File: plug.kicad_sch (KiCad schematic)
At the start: 30 parts, among them J10 Conn_01x04_GH1.25, J11 Conn_01x04_GH1.25, J12 Conn_01x04_GH1.25, J13 Conn_01x08_GH1.25, J2 Conn_01x02_XH2.54, J3 Conn_01x02_XH2.54, J4 Conn_01x02_XH2.54, J5 Conn_01x02_XH2.54, J6 KF2EDGR-3.81-2P, J7 Conn_01x04_GH1.25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

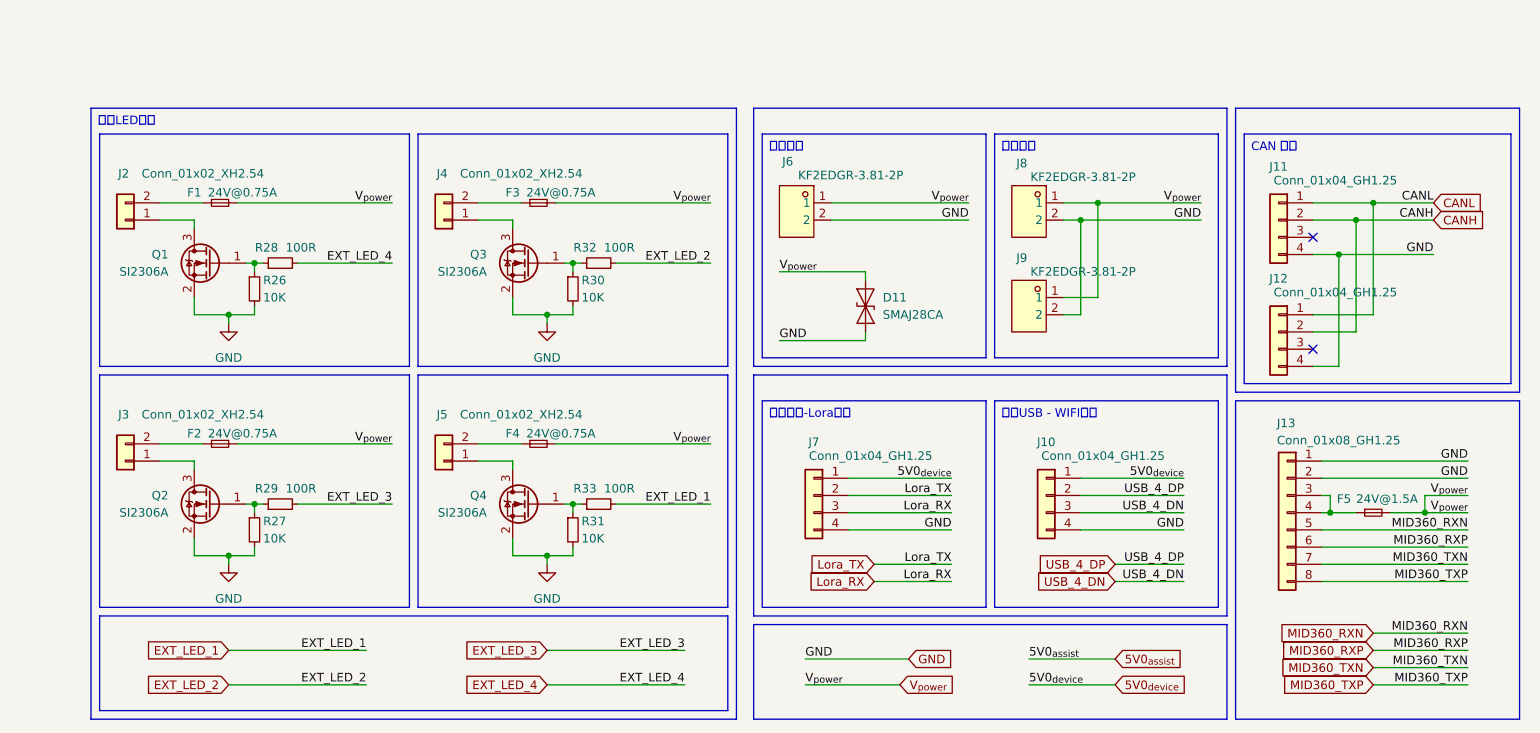
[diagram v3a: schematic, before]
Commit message: pref: USB外设改自供电，优化布线
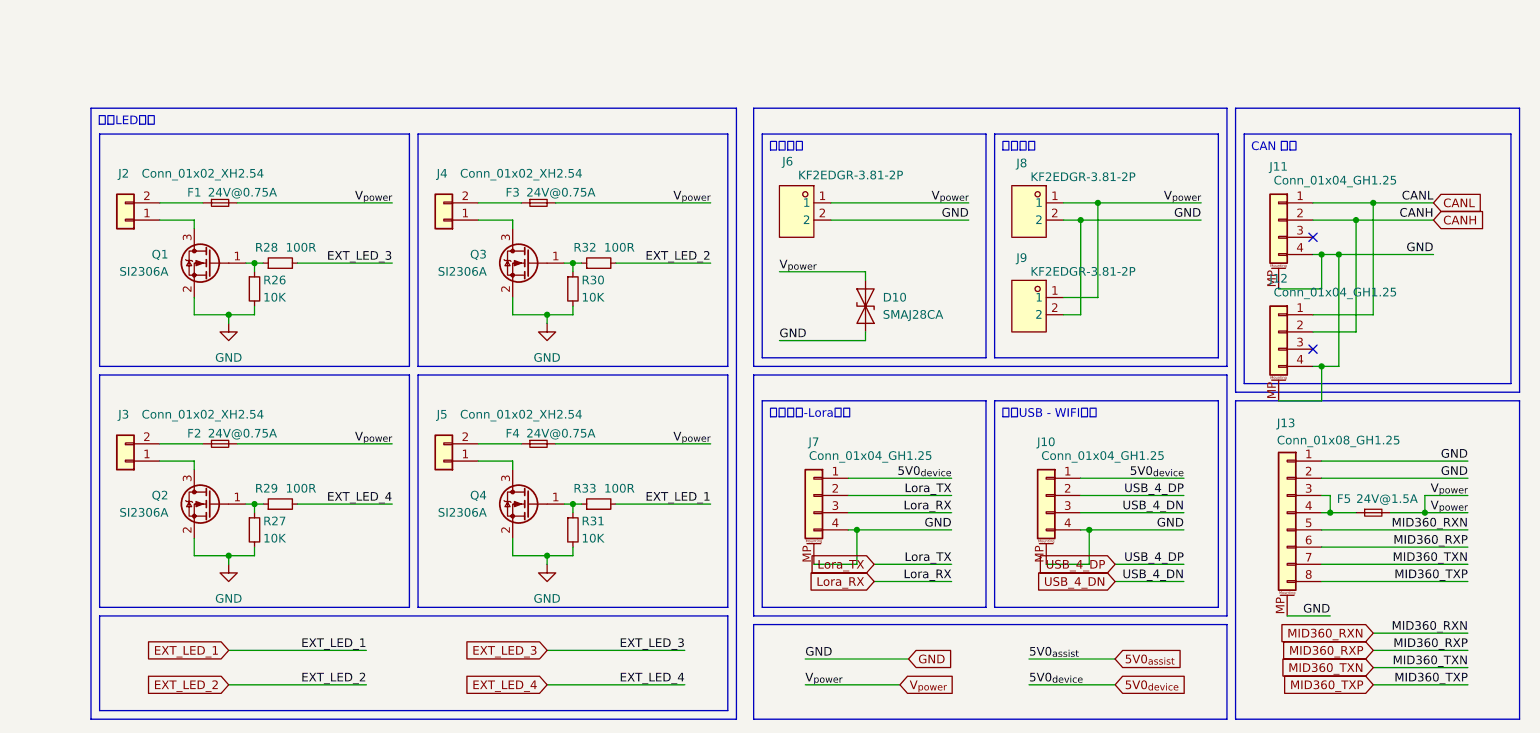
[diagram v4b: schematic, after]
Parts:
- J10, J11, J12, J7: symbol Connector_Generic:Conn_01x04 -> Connector_Generic_MountingPin:Conn_01x04_MountingPin
- J13: symbol Connector_Generic:Conn_01x08 -> Connector_Generic_MountingPin:Conn_01x08_MountingPin
- renumbered D11 to D10
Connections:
- net EXT_LED_3: now also R28.2; no longer R29.2
- net EXT_LED_4: now also R29.2; no longer R28.2
- net GND: now also J10.MP (MountPin), J11.MP (MountPin), J12.MP (MountPin), J13.MP (MountPin), J7.MP (MountPin)
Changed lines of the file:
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@@
 	)
 	(junction
+		(at 212.09 57.15)
+		(diameter 0)
+		(color 0 0 0 0)
+	)
+	(junction
+		(at 177.8 97.79)
+		(diameter 0)
+		(color 0 0 0 0)
+	)
+	(junction
 		(at 50.8 66.04)
 		(diameter 0)
@@
 	)
 	(junction
+		(at 212.09 73.66)
+		(diameter 0)
+		(color 0 0 0 0)
+	)
+	(junction
 		(at 101.6 58.42)
 		(diameter 0)
@@
 	)
 	(junction
+		(at 143.51 97.79)
+		(diameter 0)
+		(color 0 0 0 0)
+	)
+	(junction
 		(at 219.71 49.53)
 		(diameter 0)
@@
 	(wire
 		(pts
+			(xy 212.09 62.23) (xy 212.09 57.15)
+		)
+		(stroke
+			(width 0)
+			(type default)
+		)
+	)
+	(wire
+		(pts
+			(xy 212.09 73.66) (xy 214.63 73.66)
+		)
+		(stroke
+			(width 0)
+			(type default)
+		)
+	)
+	(wire
+		(pts
 			(xy 54.61 95.25) (xy 54.61 93.98)
 		)
@@
 	(wire
 		(pts
+			(xy 212.09 105.41) (xy 233.68 105.41)
+		)
+		(stroke
+			(width 0)
+			(type default)
+		)
+	)
+	(wire
+		(pts
 			(xy 101.6 58.42) (xy 100.33 58.42)
 		)
@@
 	(wire
 		(pts
+			(xy 137.16 102.87) (xy 143.51 102.87)
+		)
+		(stroke
+			(width 0)
+			(type default)
+		)
+	)
+	(wire
+		(pts
 			(xy 99.06 49.53) (xy 121.92 49.53)
 		)
@@
 	(wire
 		(pts
-			(xy 210.82 73.66) (xy 214.63 73.66)
+			(xy 210.82 73.66) (xy 212.09 73.66)
 		)
 		(stroke
@@
 	(wire
 		(pts
-			(xy 142.24 97.79) (xy 157.48 97.79)
+			(xy 142.24 97.79) (xy 143.51 97.79)
 		)
 		(stroke
@@
 	(wire
 		(pts
-			(xy 60.96 93.98) (xy 74.93 93.98)
+			(xy 212.09 78.74) (xy 212.09 73.66)
 		)
 		(stroke
@@
 	(wire
 		(pts
-			(xy 219.71 66.04) (xy 219.71 49.53)
+			(xy 60.96 93.98) (xy 74.93 93.98)
 		)
 		(stroke
@@
 	(wire
 		(pts
-			(xy 212.09 105.41) (xy 233.68 105.41)
+			(xy 219.71 66.04) (xy 219.71 49.53)
 		)
 		(stroke
@@
 	(wire
 		(pts
+			(xy 171.45 102.87) (xy 177.8 102.87)
+		)
+		(stroke
+			(width 0)
+			(type default)
+		)
+	)
+	(wire
+		(pts
 			(xy 168.91 116.84) (xy 181.61 116.84)
 		)
@@
 	(wire
 		(pts
+			(xy 207.01 110.49) (xy 213.36 110.49)
+		)
+		(stroke
+			(width 0)
+			(type default)
+		)
+	)
+	(wire
+		(pts
 			(xy 179.07 63.5) (xy 179.07 49.53)
 		)
@@
 	(wire
 		(pts
+			(xy 143.51 97.79) (xy 157.48 97.79)
+		)
+		(stroke
+			(width 0)
+			(type default)
+		)
+	)
+	(wire
+		(pts
 			(xy 160.02 49.53) (xy 139.7 49.53)
 		)
@@
 	(wire
 		(pts
-			(xy 176.53 97.79) (xy 191.77 97.79)
+			(xy 176.53 97.79) (xy 177.8 97.79)
 		)
 		(stroke
@@
 	(wire
 		(pts
-			(xy 214.63 57.15) (xy 210.82 57.15)
+			(xy 214.63 57.15) (xy 212.09 57.15)
 		)
 		(stroke
@@
 	(wire
 		(pts
+			(xy 205.74 62.23) (xy 212.09 62.23)
+		)
+		(stroke
+			(width 0)
+			(type default)
+		)
+	)
+	(wire
+		(pts
+			(xy 205.74 78.74) (xy 212.09 78.74)
+		)
+		(stroke
+			(width 0)
+			(type default)
+		)
+	)
+	(wire
+		(pts
 			(xy 92.71 88.9) (xy 92.71 87.63)
 		)
@@
 	(wire
 		(pts
+			(xy 143.51 102.87) (xy 143.51 97.79)
+		)
+		(stroke
+			(width 0)
+			(type default)
+		)
+	)
+	(wire
+		(pts
 			(xy 168.91 120.65) (xy 181.61 120.65)
 		)
@@
 	(wire
 		(pts
+			(xy 177.8 97.79) (xy 191.77 97.79)
+		)
+		(stroke
+			(width 0)
+			(type default)
+		)
+	)
+	(wire
+		(pts
 			(xy 142.24 90.17) (xy 157.48 90.17)
 		)
@@
 	(wire
 		(pts
+			(xy 212.09 57.15) (xy 210.82 57.15)
+		)
+		(stroke
+			(width 0)
+			(type default)
+		)
+	)
+	(wire
+		(pts
 			(xy 194.31 49.53) (xy 179.07 49.53)
 		)
@@
 	(wire
 		(pts
+			(xy 177.8 102.87) (xy 177.8 97.79)
+		)
+		(stroke
+			(width 0)
+			(type default)
+		)
+	)
+	(wire
+		(pts
 			(xy 144.78 69.85) (xy 144.78 68.58)
 		)
@@
 	)
 	(label "EXT_LED_4"
-		(at 74.93 58.42 180)
+		(at 74.93 93.98 180)
 		(effects
 			(font
@@
 		)
 	)
+	(label "GND"
+		(at 213.36 110.49 180)
+		(effects
+			(font
+				(size 1.27 1.27)
+			)
+			(justify right bottom)
+		)
+	)
 	(label "MID360_TXP"
 		(at 233.68 120.65 180)
@@
 	)
 	(label "EXT_LED_3"
-		(at 74.93 93.98 180)
+		(at 74.93 58.42 180)
 		(effects
 			(font
@@
 	)
 	(symbol
-		(lib_id "Connector_Generic:Conn_01x04")
+		(lib_id "Connector_Generic_MountingPin:Conn_01x04_MountingPin")
 		(at 205.74 68.58 0)
 		(mirror y)
@@
 			)
 		)
-		(property "Description" "Generic connector, single row, 01x04, script generated (kicad-library-utils/schlib/autogen/connector/)"
+		(property "Description" "Generic connectable mounting pin connector, single row, 01x04, script generated (kicad-library-utils/schlib/autogen/connector/)"
 			(at 205.74 68.58 0)
 			(effects
@@
 		(pin "1"
 		)
+		(pin "MP"
+		)
 		(instances
 			(project "ZW1S"
@@
 		(dnp no)
 		(fields_autoplaced yes)
-		(property "Reference" "#PWR15"
+		(property "Reference" "#PWR16"
 			(at 97.79 73.66 0)
 			(effects
@@
 			(project "ZW1S"
 				(path "/c658c753-a869-4eb9-a520-6b2e7fae7fd9/cfdc2bd0-e52f-4e45-9f57-35a106e1bb09"
-					(reference "#PWR15")
+					(reference "#PWR16")
 					(unit 1)
 				)
@@
 		(dnp no)
 		(fields_autoplaced yes)
-		(property "Reference" "#PWR13"
+		(property "Reference" "#PWR14"
 			(at 50.8 73.66 0)
 			(effects
@@
 			(project ""
 				(path "/c658c753-a869-4eb9-a520-6b2e7fae7fd9/cfdc2bd0-e52f-4e45-9f57-35a106e1bb09"
-					(reference "#PWR13")
+					(reference "#PWR14")
 					(unit 1)
 				)
@@
 	)
 	(symbol
-		(lib_id "Connector_Generic:Conn_01x04")
+		(lib_id "Connector_Generic_MountingPin:Conn_01x04_MountingPin")
 		(at 171.45 92.71 0)
 		(mirror y)
@@
 			)
 		)
-		(property "Description" "Generic connector, single row, 01x04, script generated (kicad-library-utils/schlib/autogen/connector/)"
+		(property "Description" "Generic connectable mounting pin connector, single row, 01x04, script generated (kicad-library-utils/schlib/autogen/connector/)"
 			(at 171.45 92.71 0)
 			(effects
@@
 		(pin "1"
 		)
+		(pin "MP"
+		)
 		(instances
 			(project "ZW1S"
@@
 		(dnp no)
 		(fields_autoplaced yes)
-		(property "Reference" "#PWR16"
+		(property "Reference" "#PWR17"
 			(at 97.79 109.22 0)
 			(effects
@@
 			(project "ZW1S"
 				(path "/c658c753-a869-4eb9-a520-6b2e7fae7fd9/cfdc2bd0-e52f-4e45-9f57-35a106e1bb09"
-					(reference "#PWR16")
+					(reference "#PWR17")
 					(unit 1)
 				)
@@
 	)
 	(symbol
-		(lib_id "Connector_Generic:Conn_01x04")
+		(lib_id "Connector_Generic_MountingPin:Conn_01x04_MountingPin")
 		(at 205.74 52.07 0)
 		(mirror y)
@@
 			)
 		)
-		(property "Description" "Generic connector, single row, 01x04, script generated (kicad-library-utils/schlib/autogen/connector/)"
+		(property "Description" "Generic connectable mounting pin connector, single row, 01x04, script generated (kicad-library-utils/schlib/autogen/connector/)"
 			(at 205.74 52.07 0)
 			(effects
@@
 		(pin "1"
 		)
+		(pin "MP"
+		)
 		(instances
 			(project ""
@@
 		(dnp no)
 		(fields_autoplaced yes)
-		(property "Reference" "D11"
+		(property "Reference" "D10"
 			(at 147.32 63.4999 90)
 			(effects
@@
 			(project "ZW1S"
 				(path "/c658c753-a869-4eb9-a520-6b2e7fae7fd9/cfdc2bd0-e52f-4e45-9f57-35a106e1bb09"
-					(reference "D11")
+					(reference "D10")
 					(unit 1)
 				)
@@
 	)
 	(symbol
-		(lib_id "Connector_Generic:Conn_01x08")
+		(lib_id "Connector_Generic_MountingPin:Conn_01x08_MountingPin")
 		(at 207.01 95.25 0)
 		(mirror y)
@@
 			)
 		)
-		(property "Description" "Generic connector, single row, 01x08, script generated (kicad-library-utils/schlib/autogen/connector/)"
+		(property "Description" "Generic connectable mounting pin connector, single row, 01x08, script generated (kicad-library-utils/schlib/autogen/connector/)"
 			(at 207.01 95.25 0)
 			(effects
@@
 		(pin "5"
 		)
+		(pin "MP"
+		)
 		(instances
 			(project ""
@@
 		(dnp no)
 		(fields_autoplaced yes)
-		(property "Reference" "#PWR14"
+		(property "Reference" "#PWR15"
 			(at 50.8 109.22 0)
 			(effects
@@
 			(project "ZW1S"
 				(path "/c658c753-a869-4eb9-a520-6b2e7fae7fd9/cfdc2bd0-e52f-4e45-9f57-35a106e1bb09"
-					(reference "#PWR14")
+					(reference "#PWR15")
 					(unit 1)
 				)
@@
 	)
 	(symbol
-		(lib_id "Connector_Generic:Conn_01x04")
+		(lib_id "Connector_Generic_MountingPin:Conn_01x04_MountingPin")
 		(at 137.16 92.71 0)
 		(mirror y)
@@
 			)
 		)
-		(property "Description" "Generic connector, single row, 01x04, script generated (kicad-library-utils/schlib/autogen/connector/)"
+		(property "Description" "Generic connectable mounting pin connector, single row, 01x04, script generated (kicad-library-utils/schlib/autogen/connector/)"
 			(at 137.16 92.71 0)
 			(effects
@@
 		(pin "1"
 		)
+		(pin "MP"
+		)
 		(instances
